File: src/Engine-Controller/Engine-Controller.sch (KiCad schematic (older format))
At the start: 0 parts

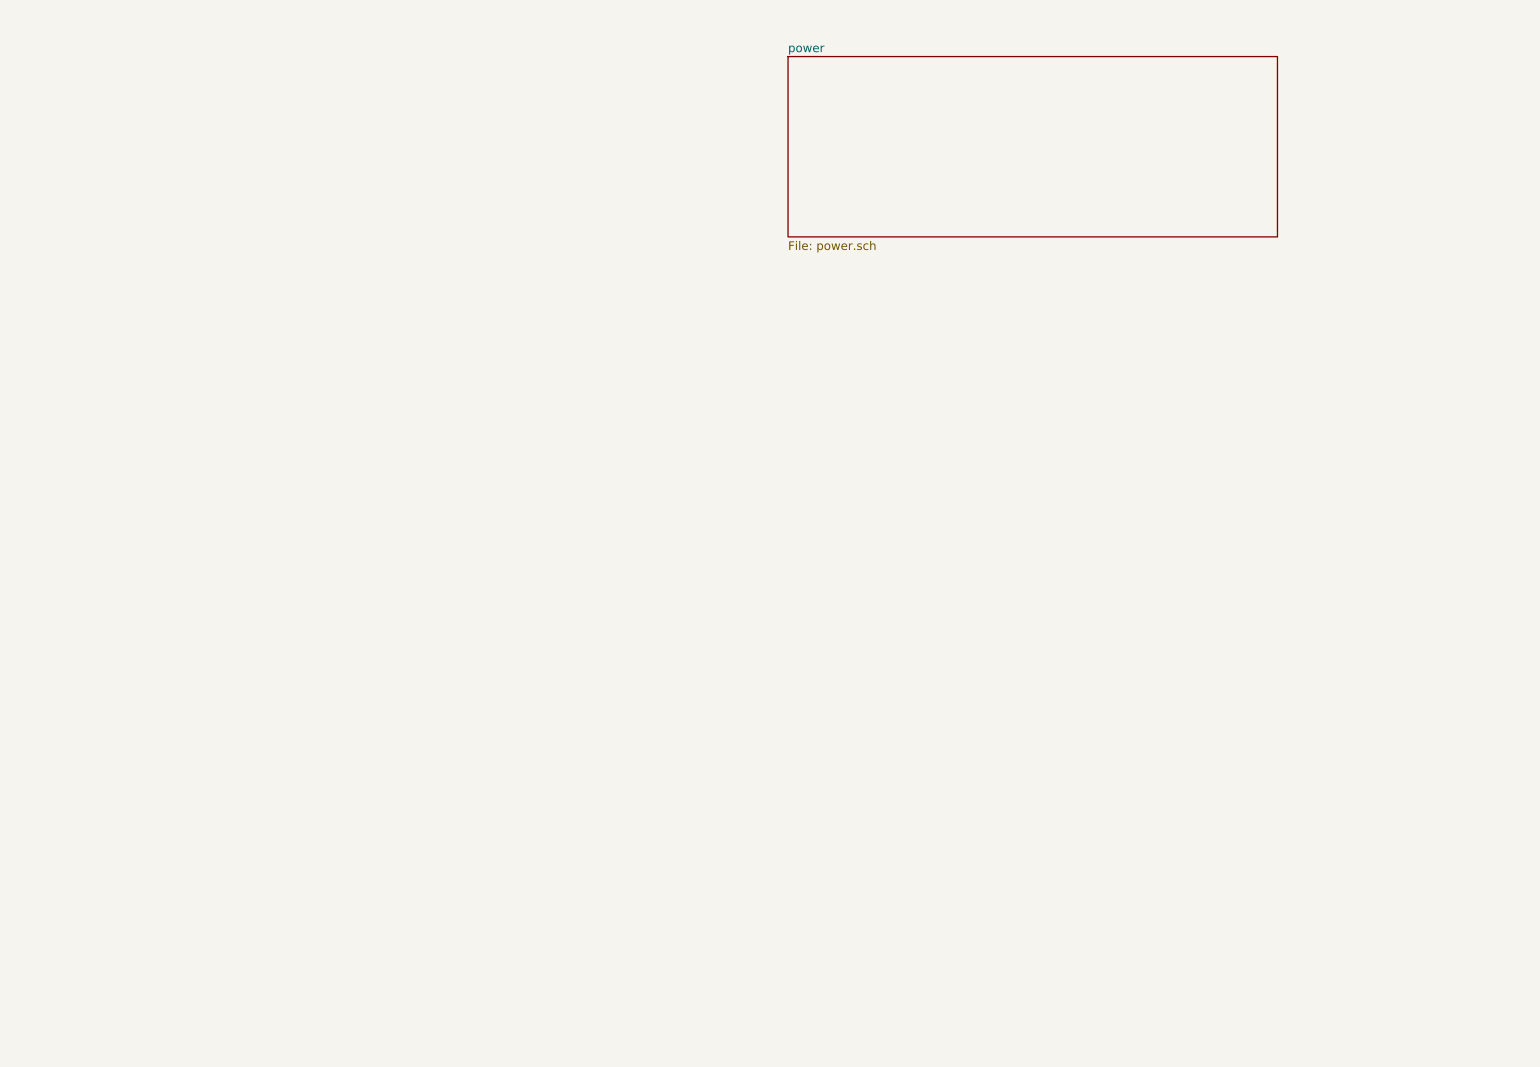
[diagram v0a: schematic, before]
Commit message: Added testpoints to library files
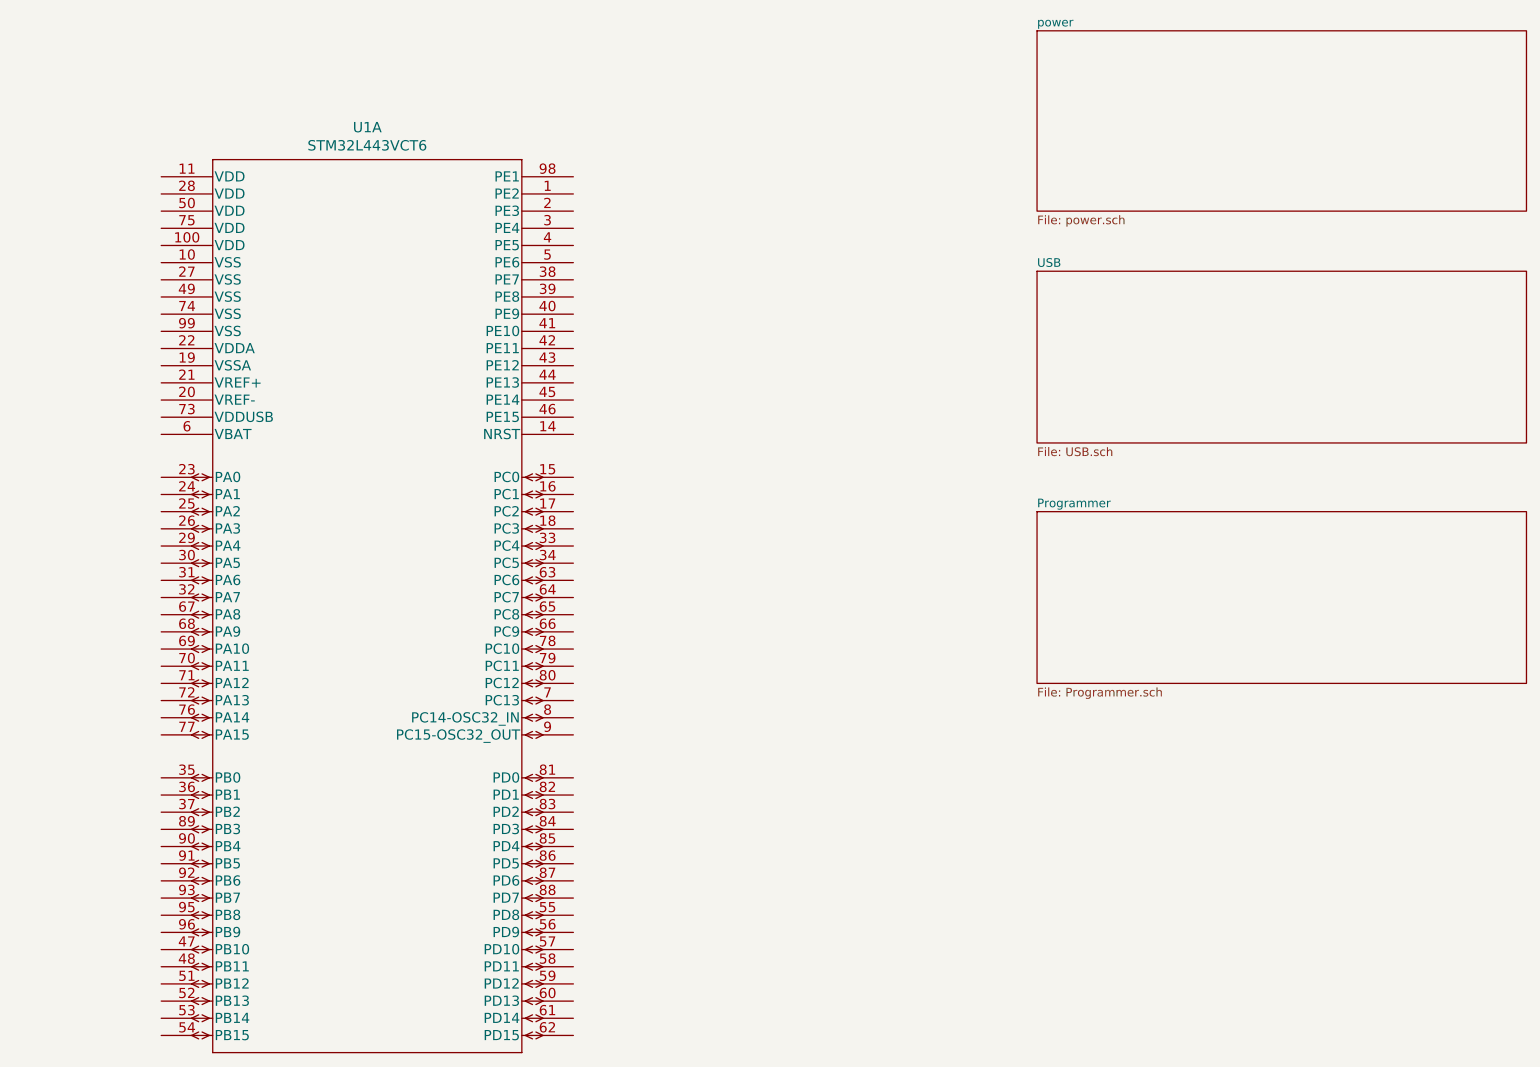
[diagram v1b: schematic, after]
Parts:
- added U1: STM32L443VCT6, Engine-Controller:STM32L443VCT6, symbol Engine-Controller:STM32L443VCT6
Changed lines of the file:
@@
 $Descr A4 11693 8268
 encoding utf-8
-Sheet 1 2
+Sheet 1 4
 Title "Engine Controller Microcontroller Board"
 Date "2021-06-26"
@@
 $EndDescr
 $Sheet
-S 6650 900  2850 1050
+S 8100 750  2850 1050
 U 60D7F309
 F0 "power" 50
 F1 "power.sch" 50
 $EndSheet
+$Sheet
+S 8100 2150 2850 1000
+U 60DAA9B3
+F0 "USB" 50
+F1 "USB.sch" 50
+$EndSheet
+$Sheet
+S 8100 3550 2850 1000
+U 60DAAA3E
+F0 "Programmer" 50
+F1 "Programmer.sch" 50
+$EndSheet
+$Comp
+L Engine-Controller:STM32L443VCT6 U1
+U 1 1 60DAAAAD
+P 4100 5350
+F 0 "U1" H 4200 9387 60  0000 C CNN
+F 1 "STM32L443VCT6" H 4200 9281 60  0000 C CNN
+F 2 "Engine-Controller:STM32L443VCT6" H 4100 9300 60  0001 C CNN
+F 3 "" H 3000 7350 60  0000 C CNN
+	1    4100 5350
+	1    0    0    -1
+$EndComp
 $EndSCHEMATC

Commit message: Completed power supply part of schematic
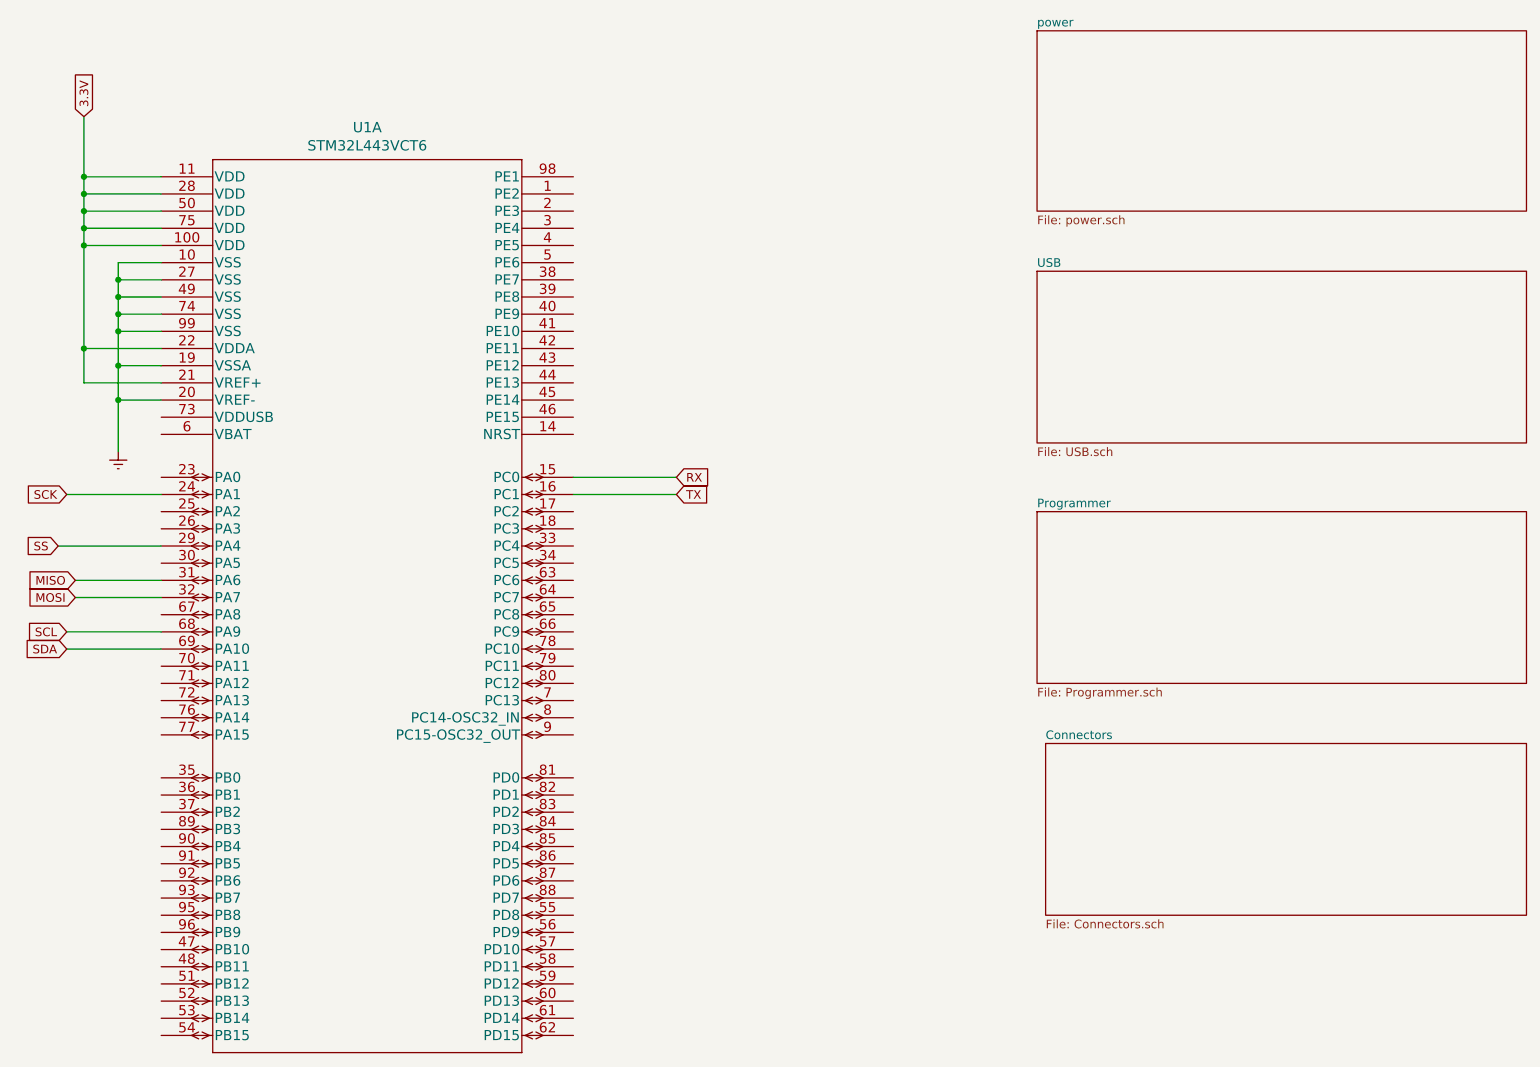
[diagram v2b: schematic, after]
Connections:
- net Earth: now reaches U1.10 (VSS)
- net Earth: now also U1.19 (VSSA), U1.20 (VREF-), U1.27 (VSS), U1.49 (VSS), U1.74 (VSS), U1.99 (VSS)
- net 3.3V: now reaches U1.100 (VDD)
- net 3.3V: now also U1.11 (VDD), U1.21 (VREF+), U1.22 (VDDA), U1.28 (VDD), U1.50 (VDD), U1.75 (VDD)
- net RX: now reaches U1.15 (PC0)
- net TX: now reaches U1.16 (PC1)
- net SCK: now reaches U1.24 (PA1)
- net SS: now reaches U1.29 (PA4)
- net MISO: now reaches U1.31 (PA6)
- net MOSI: now reaches U1.32 (PA7)
- net SCL: now reaches U1.68 (PA9)
- net SDA: now reaches U1.69 (PA10)
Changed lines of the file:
@@
 $Descr A4 11693 8268
 encoding utf-8
-Sheet 1 4
+Sheet 1 5
 Title "Engine Controller Microcontroller Board"
 Date "2021-06-26"
@@
 	1    0    0    -1
 $EndComp
+$Sheet
+S 8150 4900 2800 1000
+U 60E24895
+F0 "Connectors" 50
+F1 "Connectors.sch" 50
+$EndSheet
+Text GLabel 6000 3350 2    50   Input ~ 0
+RX
+Text GLabel 6000 3450 2    50   Input ~ 0
+TX
+Text GLabel 2500 4050 0    50   Input ~ 0
+MOSI
+Text GLabel 2500 3950 0    50   Input ~ 0
+MISO
+Text GLabel 2450 3450 0    50   Input ~ 0
+SCK
+Text GLabel 2450 4350 0    50   Input ~ 0
+SDA
+Text GLabel 2450 4250 0    50   Input ~ 0
+SCL
+Text GLabel 2400 3750 0    50   Input ~ 0
+SS
+Wire Wire Line
+	5400 3350 6000 3350
+Wire Wire Line
+	5400 3450 6000 3450
+Wire Wire Line
+	3000 3950 2500 3950
+Wire Wire Line
+	3000 4050 2500 4050
+Wire Wire Line
+	2450 3450 3000 3450
+Wire Wire Line
+	2400 3750 3000 3750
+Wire Wire Line
+	2450 4250 3000 4250
+Wire Wire Line
+	3000 4350 2450 4350
+Text GLabel 2550 1250 1    50   Input ~ 0
+3.3V
+Wire Wire Line
+	2550 1250 2550 1600
+Wire Wire Line
+	2550 1600 3000 1600
+Wire Wire Line
+	2550 1600 2550 1700
+Wire Wire Line
+	2550 1700 3000 1700
+Connection ~ 2550 1600
+Wire Wire Line
+	2550 1700 2550 1800
+Wire Wire Line
+	2550 1800 3000 1800
+Connection ~ 2550 1700
+Wire Wire Line
+	2550 1800 2550 1900
+Wire Wire Line
+	2550 1900 3000 1900
+Connection ~ 2550 1800
+Wire Wire Line
+	2550 1900 2550 2000
+Wire Wire Line
+	2550 2000 3000 2000
+Connection ~ 2550 1900
+Wire Wire Line
+	2550 2000 2550 2600
+Wire Wire Line
+	2550 2600 3000 2600
+Connection ~ 2550 2000
+Wire Wire Line
+	2550 2600 2550 2800
+Wire Wire Line
+	2550 2800 3000 2800
+Connection ~ 2550 2600
+$Comp
+L power:Earth #PWR?
+U 1 1 60F20D33
+P 2750 3200
+F 0 "#PWR?" H 2750 2950 50  0001 C CNN
+F 1 "Earth" H 2750 3050 50  0001 C CNN
+F 2 "" H 2750 3200 50  0001 C CNN
+F 3 "~" H 2750 3200 50  0001 C CNN
+	1    2750 3200
+	1    0    0    -1
+$EndComp
+Wire Wire Line
+	3000 2900 2750 2900
+Wire Wire Line
+	2750 2900 2750 3200
+Wire Wire Line
+	3000 2700 2750 2700
+Wire Wire Line
+	2750 2700 2750 2900
+Connection ~ 2750 2900
+Wire Wire Line
+	3000 2500 2750 2500
+Connection ~ 2750 2700
+Wire Wire Line
+	3000 2400 2750 2400
+Connection ~ 2750 2500
+Wire Wire Line
+	2750 2500 2750 2700
+Wire Wire Line
+	3000 2300 2750 2300
+Wire Wire Line
+	2750 2300 2750 2400
+Connection ~ 2750 2400
+Wire Wire Line
+	2750 2400 2750 2500
+Wire Wire Line
+	3000 2200 2750 2200
+Wire Wire Line
+	2750 2200 2750 2300
+Connection ~ 2750 2300
+Wire Wire Line
+	3000 2100 2750 2100
+Wire Wire Line
+	2750 2100 2750 2200
+Connection ~ 2750 2200
 $EndSCHEMATC

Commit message: Annotated Schematic
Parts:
- added D1: 150120AS75000, symbol Engine-Controller:150120AS75000
- added R1: 240, symbol Engine-Controller:RES_0603
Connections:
- net Earth: now also R1.2
- net at U1.1 (PE2): now also D1.2
- net RST: now reaches U1.14 (NRST)
- net IO9: now reaches U1.55 (PD8)
- net IO10: now reaches U1.56 (PD9)
- net SWDIO: now reaches U1.72 (PA13)
- net SWCLK: now reaches U1.76 (PA14)
- net IO1: now reaches U1.81 (PD0)
- net IO2: now reaches U1.82 (PD1)
- net IO3: now reaches U1.83 (PD2)
- net IO4: now reaches U1.84 (PD3)
- net IO5: now reaches U1.85 (PD4)
- net IO6: now reaches U1.86 (PD5)
- net IO7: now reaches U1.87 (PD6)
- net IO8: now reaches U1.88 (PD7)
- new net: D1.1, R1.1
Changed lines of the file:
@@
 Connection ~ 2550 2600
 $Comp
-L power:Earth #PWR?
+L power:Earth #PWR0101
 U 1 1 60F20D33
 P 2750 3200
-F 0 "#PWR?" H 2750 2950 50  0001 C CNN
+F 0 "#PWR0101" H 2750 2950 50  0001 C CNN
 F 1 "Earth" H 2750 3050 50  0001 C CNN
 F 2 "" H 2750 3200 50  0001 C CNN
@@
 	2750 2100 2750 2200
 Connection ~ 2750 2200
+Text GLabel 2550 4750 0    50   Input ~ 0
+SWCLK
+Text GLabel 2550 4650 0    50   Input ~ 0
+SWDIO
+Text GLabel 6000 3100 2    50   Input ~ 0
+RST
+Wire Wire Line
+	3000 4650 2550 4650
+Wire Wire Line
+	3000 4750 2550 4750
+Wire Wire Line
+	6000 3100 5400 3100
+$Comp
+L Engine-Controller:150120AS75000 D1
+U 1 1 61009279
+P 5950 1950
+F 0 "D1" H 6179 2000 60  0000 L CNN
+F 1 "150120AS75000" H 6179 1947 60  0001 L CNN
+F 2 "" H 6150 1590 60  0001 C CNN
+F 3 "" V 5950 2200 60  0000 C CNN
+	1    5950 1950
+	1    0    0    -1
+$EndComp
+$Comp
+L Engine-Controller:RES_0603 R1
+U 1 1 6100A5B9
+P 5950 2400
+F 0 "R1" V 5904 2469 50  0000 L CNN
+F 1 "240" V 5995 2469 50  0000 L CNN
+F 2 "" H 6000 1900 50  0001 L BNN
+F 3 "" H 5950 2400 50  0001 L BNN
+	1    5950 2400
+	0    1    1    0
+$EndComp
+Wire Wire Line
+	5400 1700 5950 1700
+Wire Wire Line
+	5950 2100 5950 2200
+$Comp
+L power:Earth #PWR0102
+U 1 1 6102ABA9
+P 5950 2750
+F 0 "#PWR0102" H 5950 2500 50  0001 C CNN
+F 1 "Earth" H 5950 2600 50  0001 C CNN
+F 2 "" H 5950 2750 50  0001 C CNN
+F 3 "~" H 5950 2750 50  0001 C CNN
+	1    5950 2750
+	1    0    0    -1
+$EndComp
+Wire Wire Line
+	5950 2600 5950 2750
+Text GLabel 6000 5100 2    50   Input ~ 0
+IO1
+Text GLabel 6000 5200 2    50   Input ~ 0
+IO2
+Text GLabel 6000 5300 2    50   Input ~ 0
+IO3
+Text GLabel 6000 5400 2    50   Input ~ 0
+IO4
+Text GLabel 6000 5500 2    50   Input ~ 0
+IO5
+Text GLabel 6000 5600 2    50   Input ~ 0
+IO6
+Text GLabel 6000 5700 2    50   Input ~ 0
+IO7
+Text GLabel 6000 5800 2    50   Input ~ 0
+IO8
+Text GLabel 6000 5900 2    50   Input ~ 0
+IO9
+Text GLabel 5950 6000 2    50   Input ~ 0
+IO10
+Wire Wire Line
+	6000 5100 5400 5100
+Wire Wire Line
+	6000 5200 5400 5200
+Wire Wire Line
+	6000 5300 5400 5300
+Wire Wire Line
+	6000 5400 5400 5400
+Wire Wire Line
+	6000 5500 5400 5500
+Wire Wire Line
+	6000 5600 5400 5600
+Wire Wire Line
+	6000 5700 5400 5700
+Wire Wire Line
+	6000 5800 5400 5800
+Wire Wire Line
+	6000 5900 5400 5900
+Wire Wire Line
+	5950 6000 5400 6000
 $EndSCHEMATC

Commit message: Associated Schematic Symbols with footprints
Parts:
- D1: footprint (none) -> Engine-Controller:150120AS75000
- R1: footprint (none) -> Engine-Controller:RES_0603
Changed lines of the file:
@@
 F 0 "D1" H 6179 2000 60  0000 L CNN
 F 1 "150120AS75000" H 6179 1947 60  0001 L CNN
-F 2 "" H 6150 1590 60  0001 C CNN
+F 2 "Engine-Controller:150120AS75000" H 6150 1590 60  0001 C CNN
 F 3 "" V 5950 2200 60  0000 C CNN
 	1    5950 1950
@@
 F 0 "R1" V 5904 2469 50  0000 L CNN
 F 1 "240" V 5995 2469 50  0000 L CNN
-F 2 "" H 6000 1900 50  0001 L BNN
+F 2 "Engine-Controller:RES_0603" H 6000 1900 50  0001 L BNN
 F 3 "" H 5950 2400 50  0001 L BNN
 	1    5950 2400

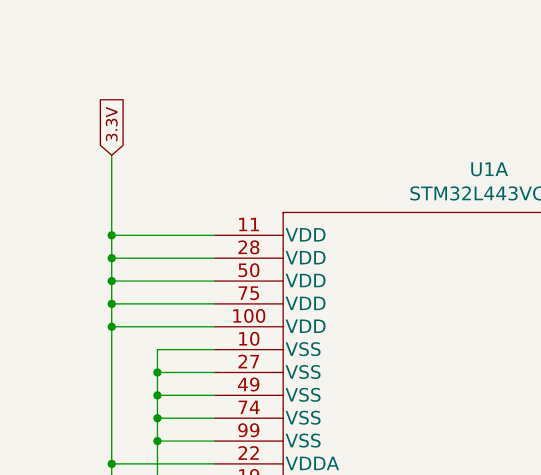
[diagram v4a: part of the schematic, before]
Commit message: Resolved all ERC issues
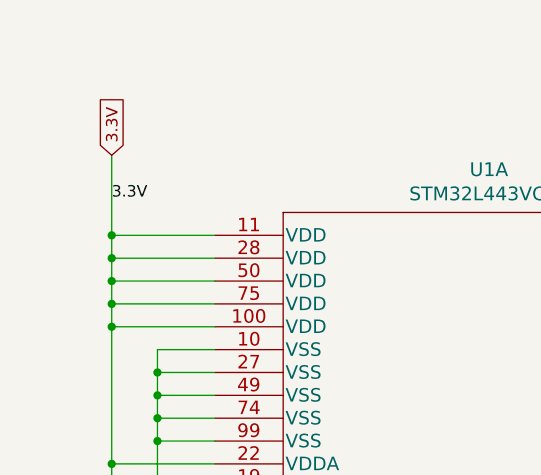
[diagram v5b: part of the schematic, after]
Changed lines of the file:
@@
 Wire Wire Line
 	5950 6000 5400 6000
+Text Label 2550 1450 0    50   ~ 0
+3.3V
 $EndSCHEMATC

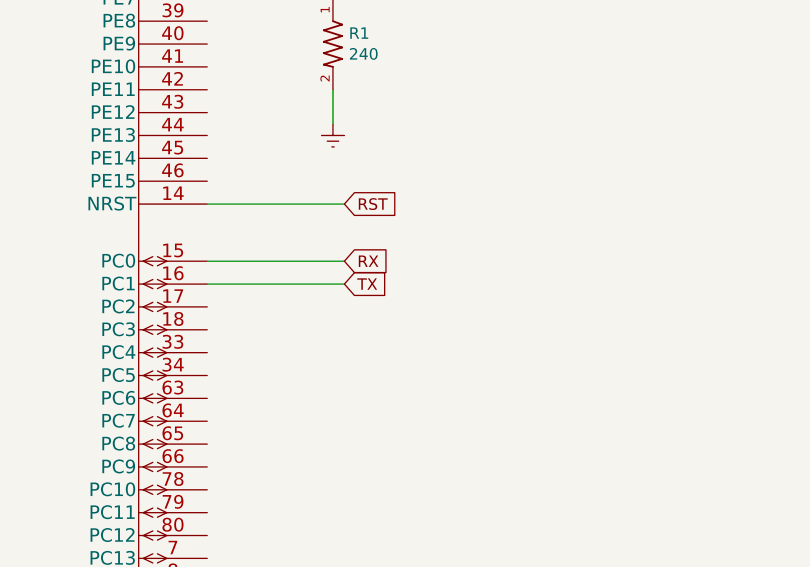
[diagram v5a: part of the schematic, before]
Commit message: Added capacitor bypassing RST to ground
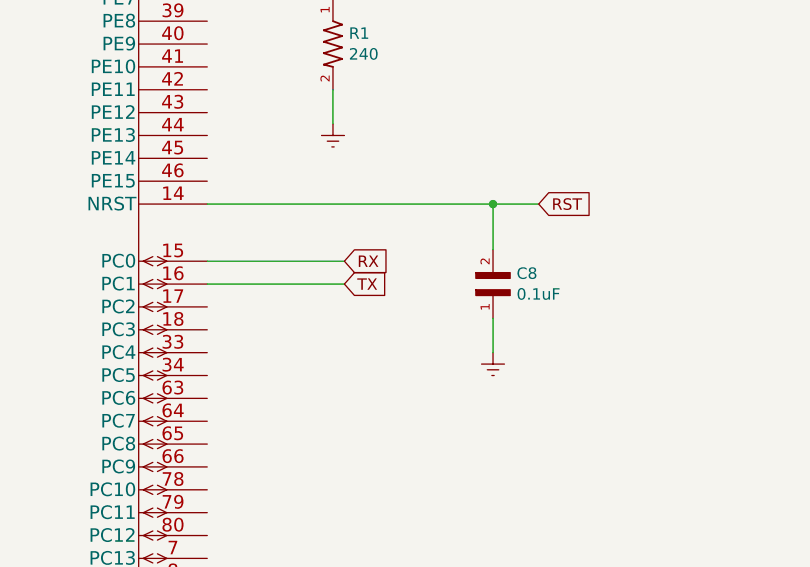
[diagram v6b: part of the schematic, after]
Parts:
- added C8: 0.1uF, Engine-Controller:CAP_0603, symbol Engine-Controller:CAP_0603
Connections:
- net Earth: now also C8.1
- net RST: now also C8.2
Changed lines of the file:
@@
 Text GLabel 2550 4650 0    50   Input ~ 0
 SWDIO
-Text GLabel 6000 3100 2    50   Input ~ 0
+Text GLabel 6850 3100 2    50   Input ~ 0
 RST
 Wire Wire Line
@@
 Wire Wire Line
 	3000 4750 2550 4750
-Wire Wire Line
-	6000 3100 5400 3100
 $Comp
 L Engine-Controller:150120AS75000 D1
@@
 Text Label 2550 1450 0    50   ~ 0
 3.3V
+Wire Wire Line
+	5400 3100 6650 3100
+$Comp
+L Engine-Controller:CAP_0603 C8
+U 1 1 60DE014C
+P 6650 3450
+F 0 "C8" V 6604 3553 50  0000 L CNN
+F 1 "0.1uF" V 6695 3553 50  0000 L CNN
+F 2 "Engine-Controller:CAP_0603" H 6550 3050 50  0001 L BNN
+F 3 "" H 6600 3450 50  0001 L BNN
+	1    6650 3450
+	0    1    1    0
+$EndComp
+$Comp
+L power:Earth #PWR01
+U 1 1 60DE602C
+P 6650 3750
+F 0 "#PWR01" H 6650 3500 50  0001 C CNN
+F 1 "Earth" H 6650 3600 50  0001 C CNN
+F 2 "" H 6650 3750 50  0001 C CNN
+F 3 "~" H 6650 3750 50  0001 C CNN
+	1    6650 3750
+	1    0    0    -1
+$EndComp
+Wire Wire Line
+	6650 3300 6650 3100
+Connection ~ 6650 3100
+Wire Wire Line
+	6650 3100 6850 3100
+Wire Wire Line
+	6650 3750 6650 3600
 $EndSCHEMATC
